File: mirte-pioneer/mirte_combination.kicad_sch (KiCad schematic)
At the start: 51 parts, among them J1 Servo3, J10 IR1, J11 Conn_01x13_Female, J12 IR Object Detector 1, J14 IR2, J17 MC1, J18 MC2, J19 Servo1, J2 Conn_01x20_Female, J20 SRF1, J21 ENC2, J23 MC1-A, J24 MC1-B, J25 SRF2, J26 ENC1, J27 Servo2, J28 I2C2, J3 Servo4, J30 I2C1, J33 line out left, J35 Power out, J37 on/off, J4 Conn_01x20_Female, J5 Conn_01x06_Pin, J7 Keypad, J8 Conn_01x06_Female, J9 IR Object Detector 2, Q1 DMG2305UX, Q2 DMN2050L, SW2 SK12D07VG5, U2 CH340E

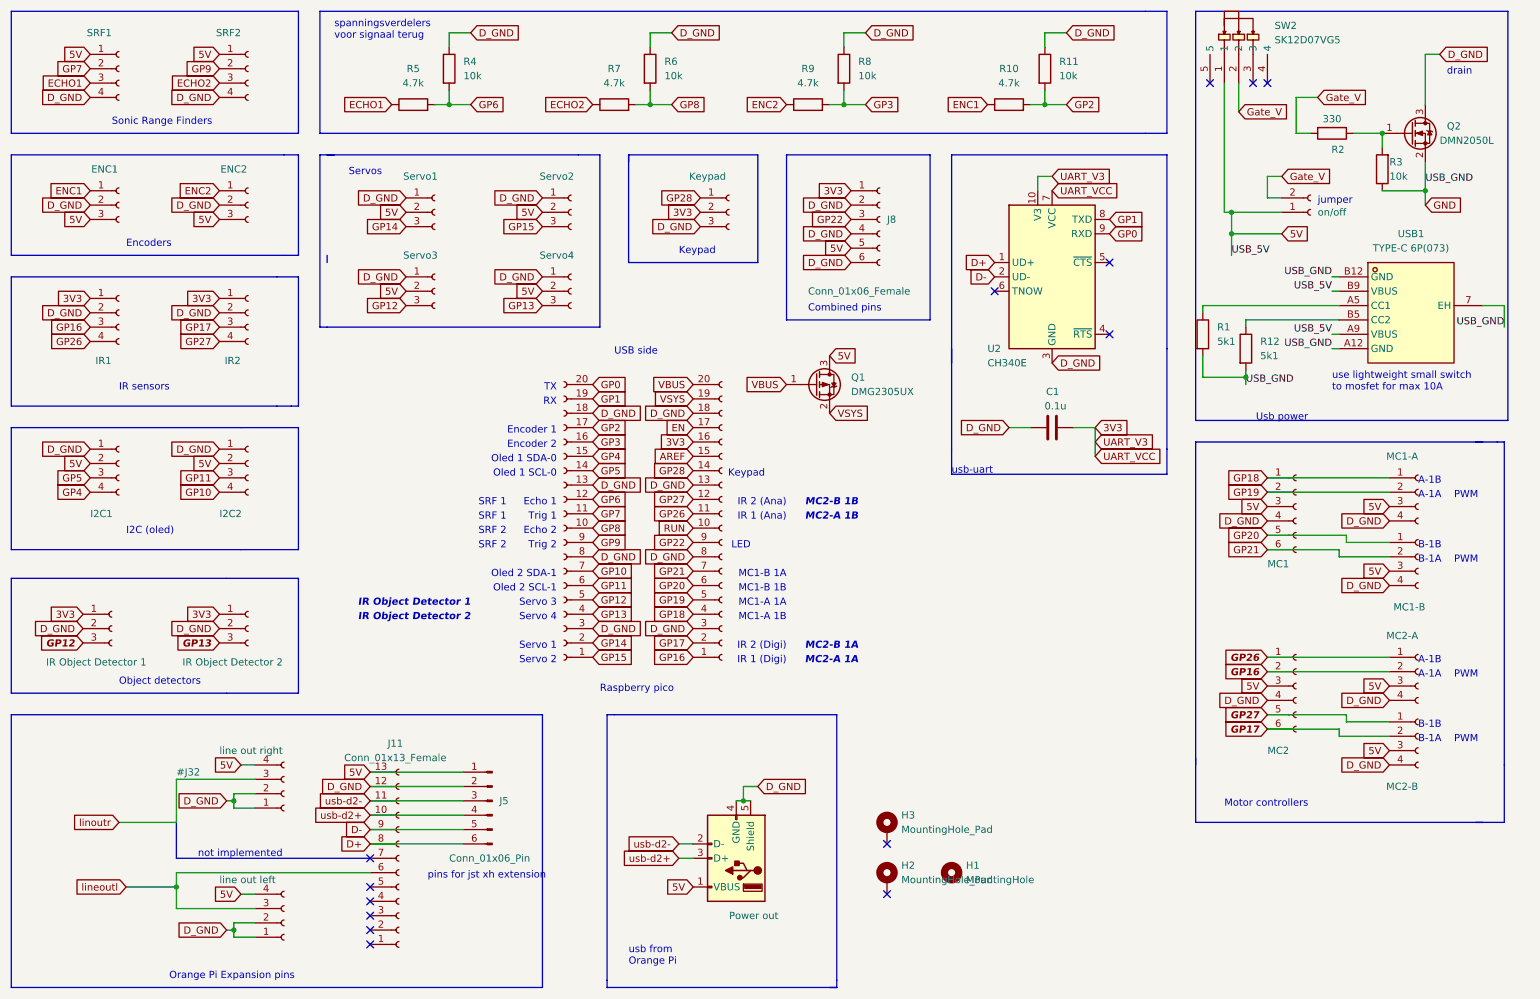
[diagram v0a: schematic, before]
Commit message: usb b micro instead of c for v0.9
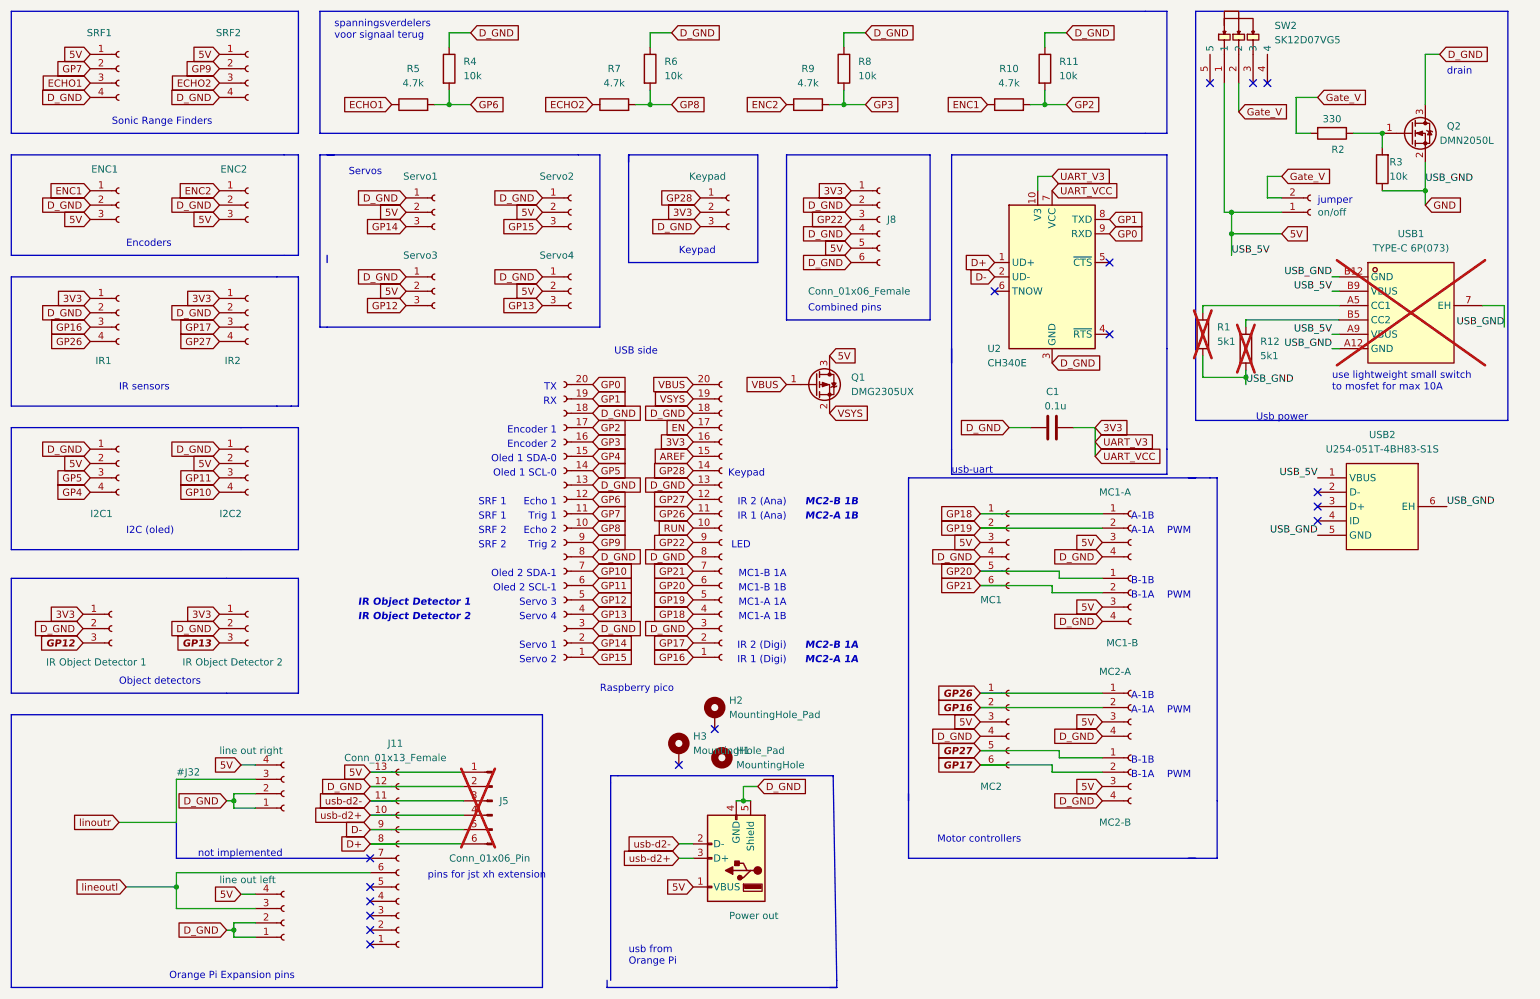
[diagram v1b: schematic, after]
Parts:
- added USB2: U254-051T-4BH83-S1S, lcsc:MICRO-USB-SMD_U254-051T-4BH83-S1S, symbol lcsc:U254-051T-4BH83-S1S
- J5, R1, R12, USB1: now not fitted; now left out of the parts list
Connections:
- net 5V: now also USB2.1 (VBUS)
- net GND: now also USB2.5 (GND), USB2.6 (EH)
- no-connect marks 14 -> 17
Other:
- moved on the sheet: H1, H2, H3

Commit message: ?
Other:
- note added: "USB B micro for Embedded Software course"
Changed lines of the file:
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@@
 	(polyline
 		(pts
-			(xy 163.195 153.035) (xy 163.83 189.23)
+			(xy 163.83 153.035) (xy 163.83 189.23)
 		)
 		(stroke
@@
 	(polyline
 		(pts
-			(xy 163.83 190.5) (xy 123.19 190.5)
+			(xy 163.83 190.5) (xy 123.825 190.5)
 		)
 		(stroke
@@
 	(polyline
 		(pts
-			(xy 125.095 153.035) (xy 163.195 153.035)
+			(xy 125.095 153.035) (xy 163.83 153.035)
 		)
 		(stroke
@@
 	(polyline
 		(pts
-			(xy 123.19 189.23) (xy 123.19 190.5)
+			(xy 123.825 189.23) (xy 123.825 190.5)
 		)
 		(stroke
@@
 		)
 	)
+	(text "USB B micro for Embedded Software course"
+		(exclude_from_sim no)
+		(at 260.35 115.57 0)
+		(effects
+			(font
+				(size 1.27 1.27)
+			)
+		)
+	)
